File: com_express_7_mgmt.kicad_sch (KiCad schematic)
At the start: 77 parts, among them J12 Plug_Bus_CE7_EPT_401-51501-51, J13 PinHeader_1x3_P2.54mm_Drill1.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, J14 PinHeader_1x3_P2.54mm_Drill1.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, Q11 BSS138-7-F, Q12 BSS138-7-F, SW1 SW_1-1825027-1_THT, U30 74AUP2G132, U31 M24C64-F_DFN8, U32 TPS3840PL30DBVR, U33 74AUP2G132, U34 LTC2950CTS8-1, U36 W25Q32FV_SOIC-8

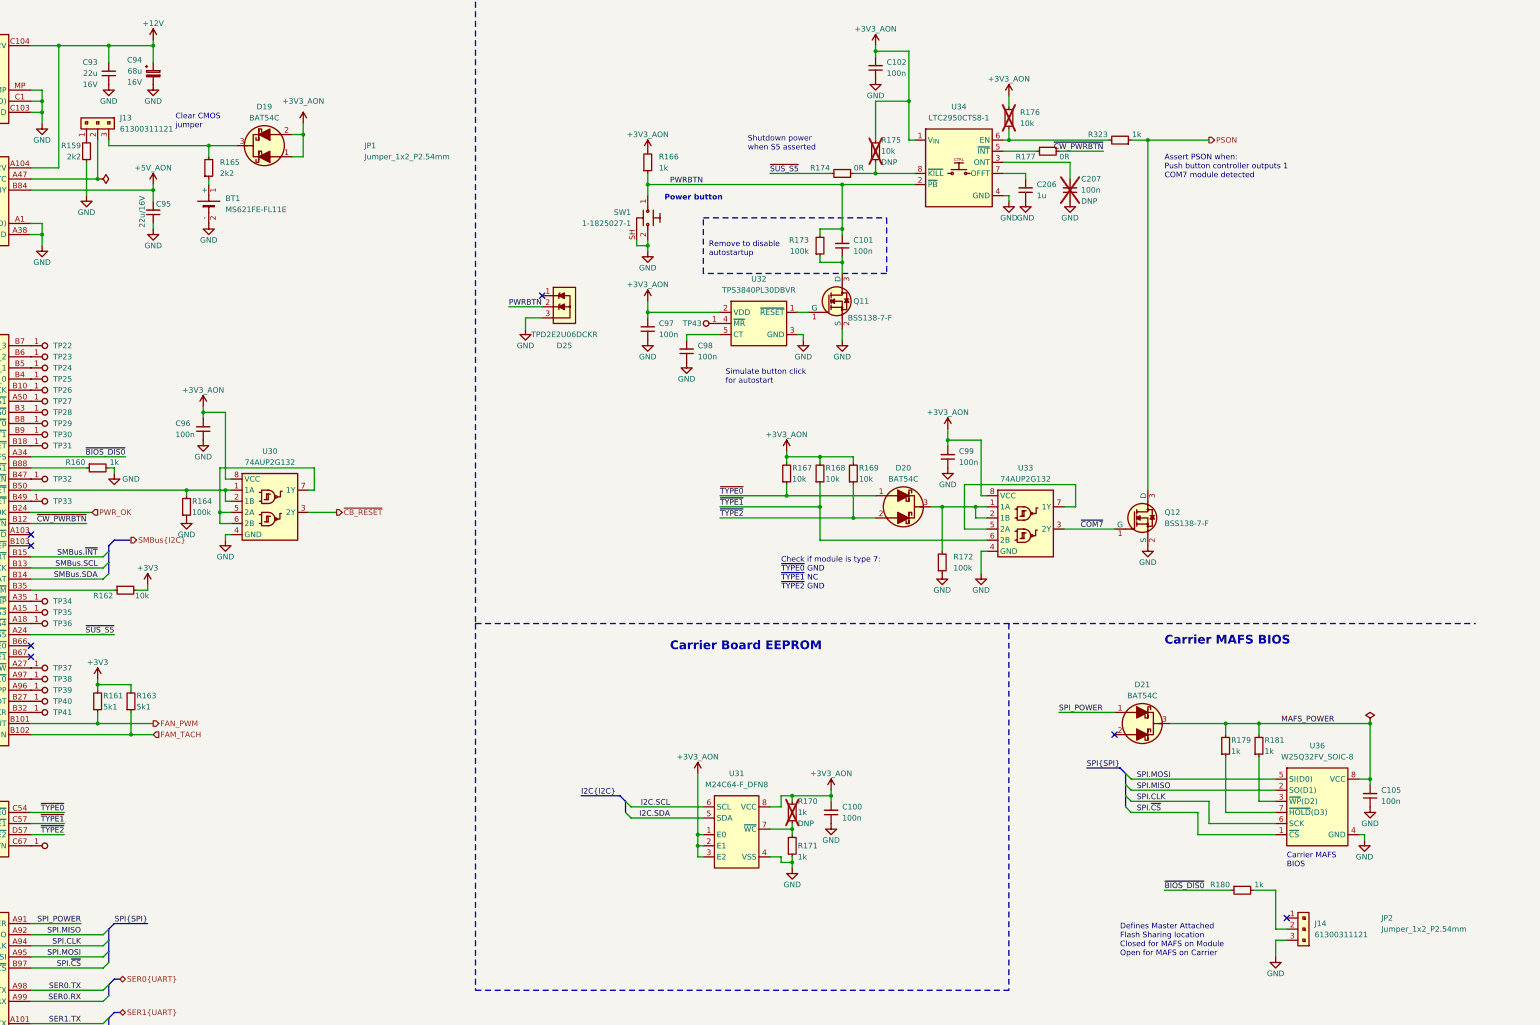
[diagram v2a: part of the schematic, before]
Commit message: Update components from the library
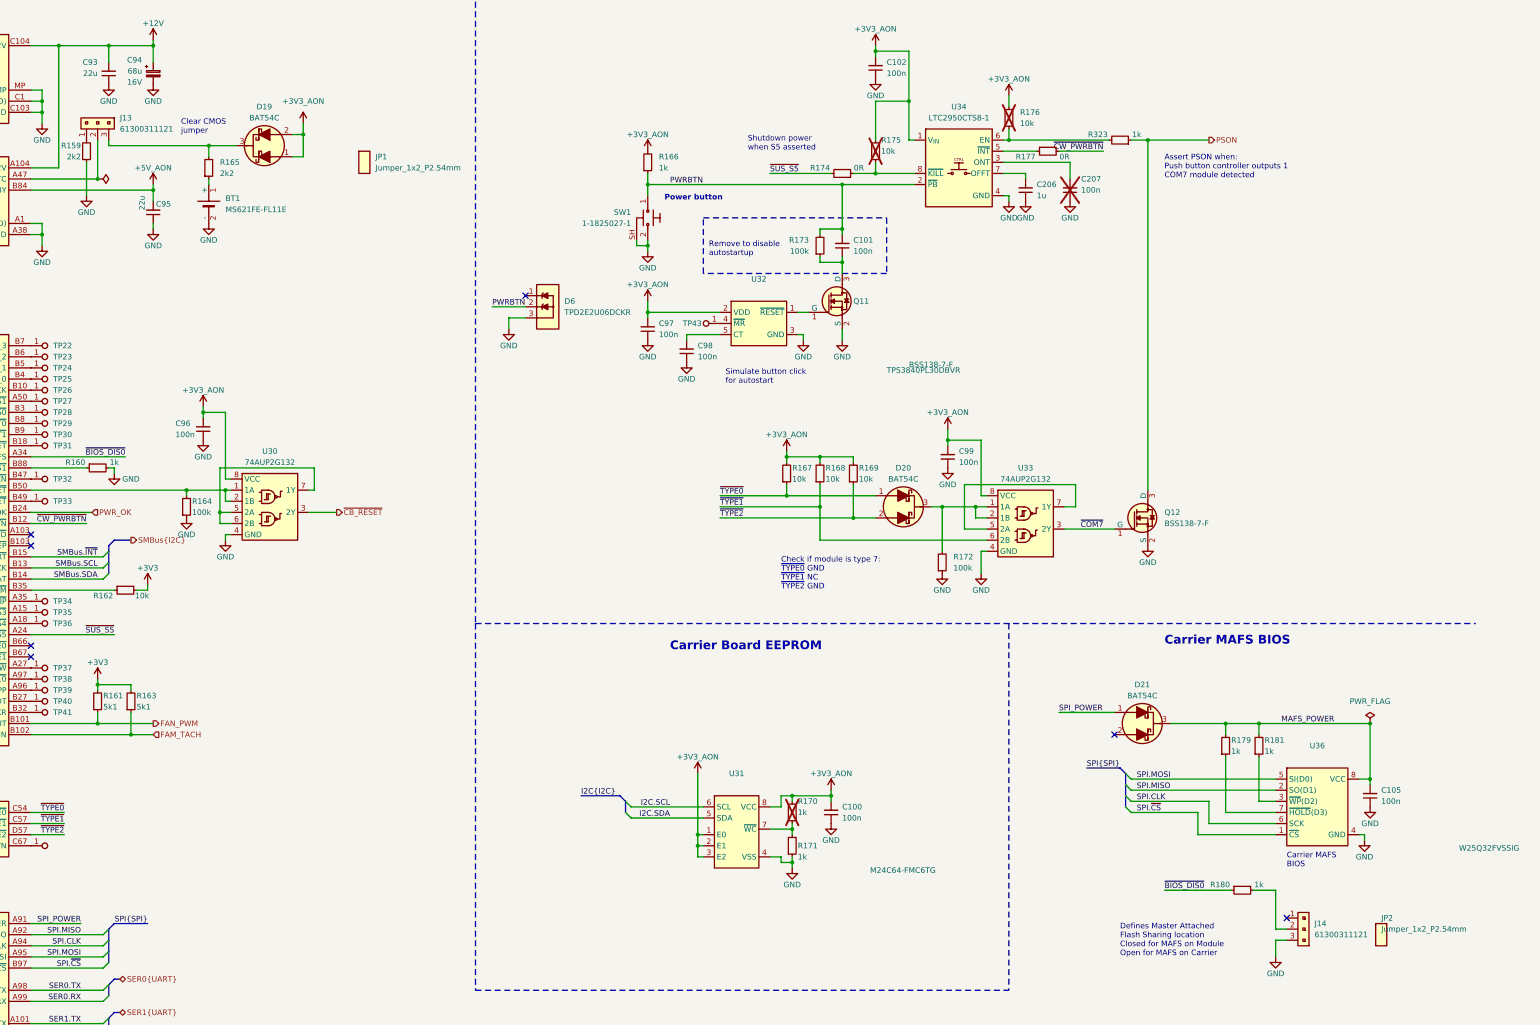
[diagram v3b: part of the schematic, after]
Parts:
- removed D25: TPD2E2U06DCKR, antmicro-footprints:SC70-3, symbol antmicroTVSDiodes:TPD2E2U06DCKR
- added D6: TPD2E2U06_SC70, antmicro-footprints:SC70-3, symbol antmicroTVSDiodes:TPD2E2U06_SC70
- C100, C101, C102, C105, C206, C93, C94, C96, C97, C98, C99, R159, R160, R161, R162, R163, R164, R165, R166, R167, R168, R169, R171, R172, R173, R174, R177, R179, R180, R181, R323, TP22, TP23, TP24, TP25, TP26, TP27, TP28, TP29, TP30, TP31, TP32, TP33, TP34, TP35, TP36, TP37, TP38, TP39, TP40, TP41, TP42, TP43: Public (none) -> False
- C207, R170, R175, R176: DNP DNP -> (none); Public (none) -> False
- C95: Public (none) -> False; Val 22u/16V -> 22u; Voltage (none) -> 16V
- J13, J14: VSD_class IO Header -> (none)
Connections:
- net GND: now also D6.3
- net PWRBTN: now also D6.2

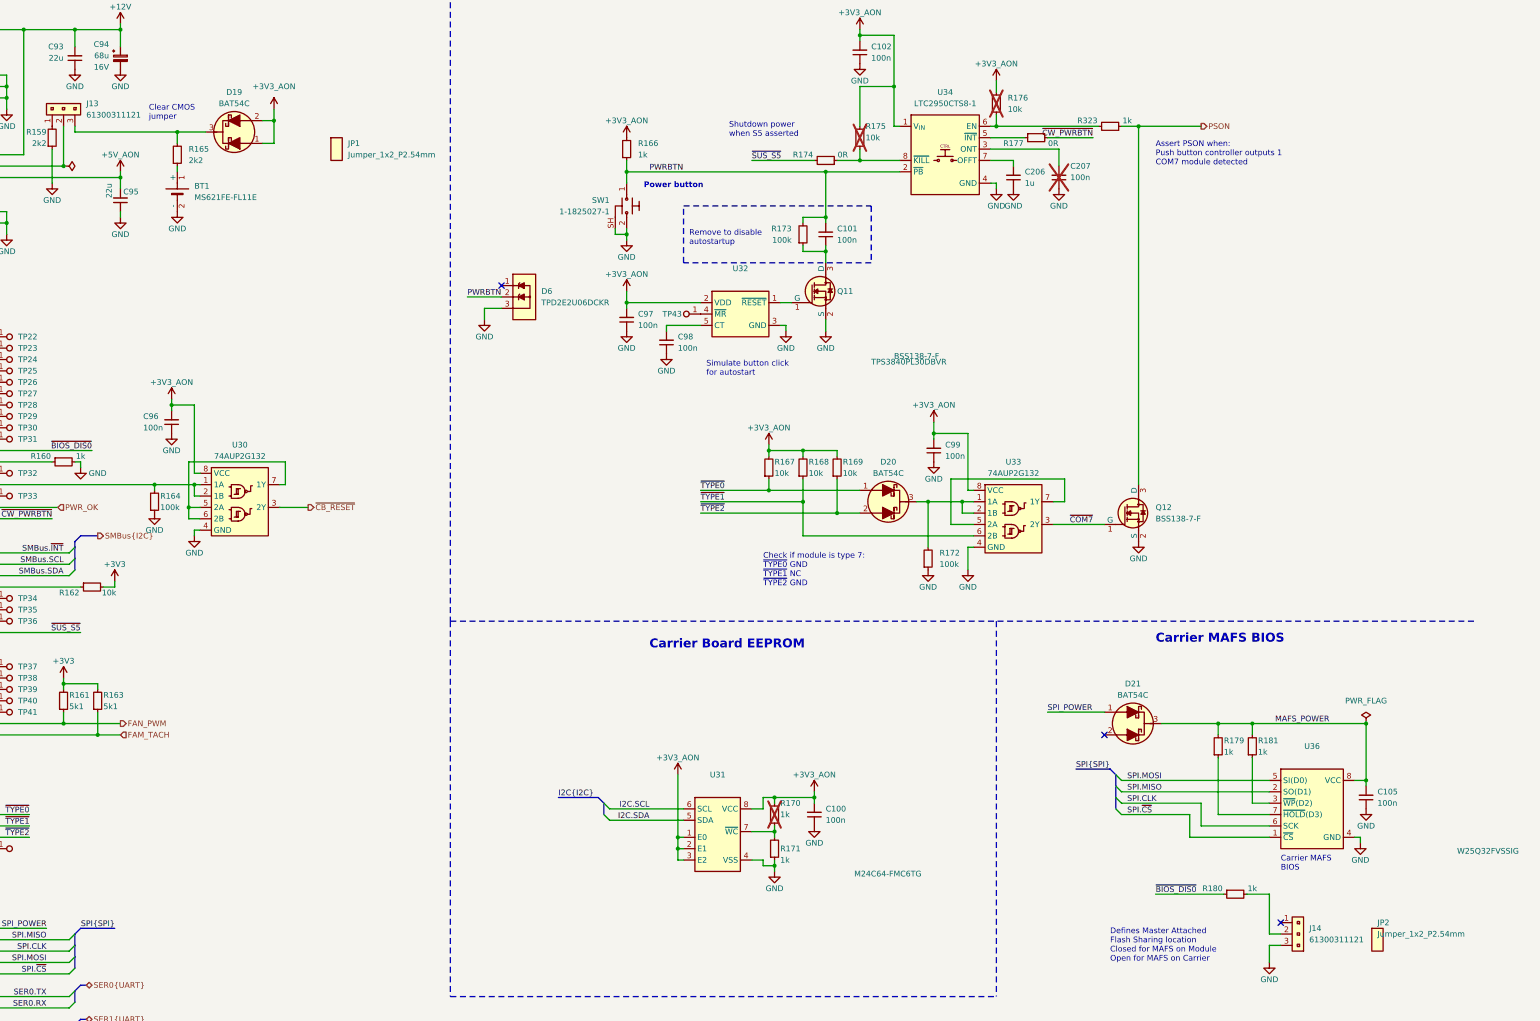
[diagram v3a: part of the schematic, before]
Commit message: [#65447] Fix rotated LEDs, overlapping text and symbols, add rules
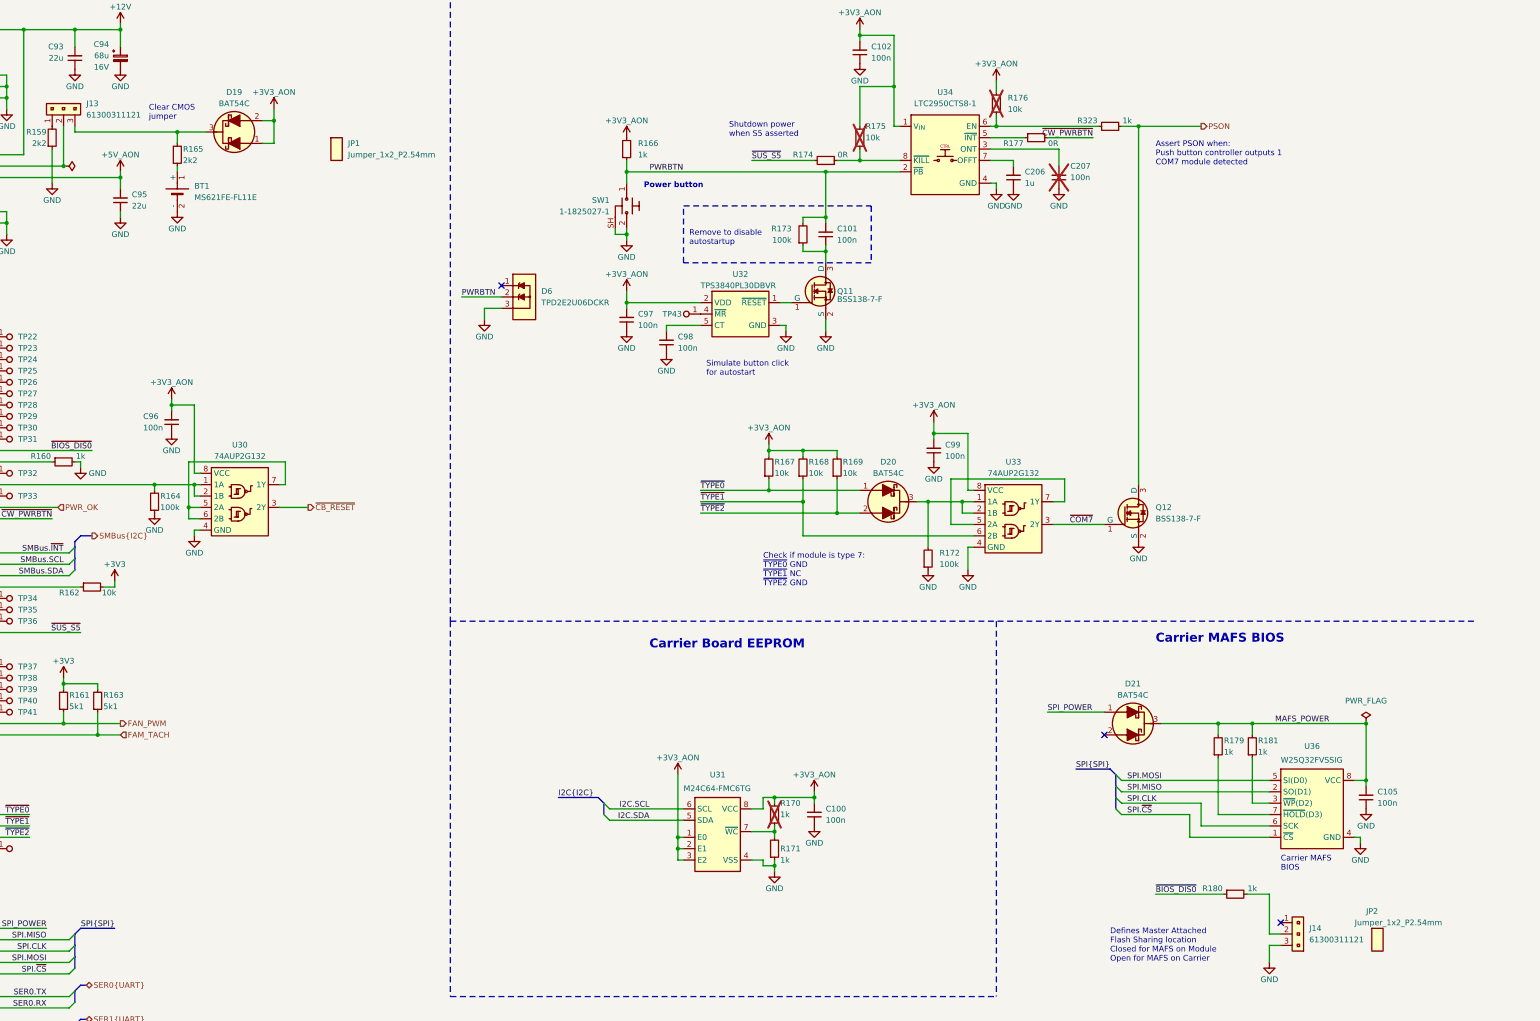
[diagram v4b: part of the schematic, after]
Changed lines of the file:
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@@
     (stroke (width 0) (type default))
   )
-  (bus (pts (xy 99.06 151.13) (xy 95.25 151.13))
+  (bus (pts (xy 97.79 151.13) (xy 95.25 151.13))
     (stroke (width 0) (type default))
   )
@@
     (stroke (width 0) (type default))
   )
-  (wire (pts (xy 181.61 97.79) (xy 189.23 97.79))
+  (wire (pts (xy 180.34 97.79) (xy 189.23 97.79))
     (stroke (width 0) (type default))
   )
@@
     (effects (font (size 1.27 1.27)) (justify right bottom))
   )
-  (label "PWRBTN" (at 181.61 97.79 0) (fields_autoplaced)
+  (label "PWRBTN" (at 180.34 97.79 0) (fields_autoplaced)
     (effects (font (size 1.27 1.27)) (justify left bottom))
   )
@@
     (effects (font (size 1.27 1.27)) (justify left))
   )
-  (hierarchical_label "SMBus{I2C}" (shape output) (at 99.06 151.13 0) (fields_autoplaced)
+  (hierarchical_label "SMBus{I2C}" (shape output) (at 97.79 151.13 0) (fields_autoplaced)
     (effects (font (size 1.27 1.27)) (justify left))
   )
@@
   )
   (symbol (lib_id "antmicroMemory:W25Q32FV_SOIC-8") (at 360.68 205.74 0) (unit 1)
-    (in_bom yes) (on_board yes) (dnp no) (fields_autoplaced)
+    (in_bom yes) (on_board yes) (dnp no)
     (property "Reference" "U36" (at 370.205 198.12 0)
       (effects (font (size 1.27 1.27) (thickness 0.15)))
@@
       (effects (font (size 1.27 1.27) (thickness 0.15)) (justify left bottom) hide)
     )
-    (property "MPN" "W25Q32FVSSIG" (at 402.59 222.25 0)
+    (property "MPN" "W25Q32FVSSIG" (at 363.22 201.93 0)
       (effects (font (size 1.27 1.27) (thickness 0.15)) (justify left bottom))
     )
@@
   )
   (symbol (lib_id "antmicroCapacitors0603:C_22u_16V_0603") (at 104.14 78.74 90) (unit 1)
-    (in_bom yes) (on_board yes) (dnp no)
-    (property "Reference" "C95" (at 104.775 74.295 90)
+    (in_bom yes) (on_board yes) (dnp no) (fields_autoplaced)
+    (property "Reference" "C95" (at 106.68 74.9236 90)
       (effects (font (size 1.27 1.27) (thickness 0.15)) (justify right))
     )
@@
       (effects (font (size 1.27 1.27) (thickness 0.15)) (justify left bottom) hide)
     )
-    (property "Val" "22u" (at 101.6 72.39 0)
+    (property "Val" "22u" (at 106.68 77.4636 90)
       (effects (font (size 1.27 1.27) (thickness 0.15)) (justify right))
     )
@@
   (symbol (lib_id "antmicroBatteryHoldersClipsContacts:Battery_Holder_MS621FE-FL11E") (at 116.84 69.85 0) (unit 1)
     (in_bom yes) (on_board yes) (dnp no) (fields_autoplaced)
-    (property "Reference" "BT1" (at 120.65 73.0249 0)
+    (property "Reference" "BT1" (at 120.65 73.025 0)
       (effects (font (size 1.27 1.27) (thickness 0.15)) (justify left))
     )
@@
       (effects (font (size 1.27 1.27) (thickness 0.15)) (justify left bottom) hide)
     )
-    (property "MPN" "MS621FE-FL11E" (at 120.65 75.5649 0)
+    (property "MPN" "MS621FE-FL11E" (at 120.65 75.565 0)
       (effects (font (size 1.27 1.27) (thickness 0.15)) (justify left))
     )
@@
       (effects (font (size 1.27 1.27) (thickness 0.15)) (justify left bottom) hide)
     )
-    (property "MPN" "BSS138-7-F" (at 276.86 111.76 0)
+    (property "MPN" "BSS138-7-F" (at 264.16 99.06 0)
       (effects (font (size 1.27 1.27) (thickness 0.15)) (justify left bottom))
     )
@@
   )
   (symbol (lib_id "antmicroMemory:M24C64-F_DFN8") (at 229.87 212.09 0) (unit 1)
-    (in_bom yes) (on_board yes) (dnp no) (fields_autoplaced)
+    (in_bom yes) (on_board yes) (dnp no)
     (property "Reference" "U31" (at 237.49 204.47 0)
       (effects (font (size 1.27 1.27) (thickness 0.15)))
@@
       (effects (font (size 1.27 1.27) (thickness 0.15)) (justify left bottom) hide)
     )
-    (property "MPN" "M24C64-FMC6TG" (at 267.97 227.33 0)
+    (property "MPN" "M24C64-FMC6TG" (at 229.87 208.28 0)
       (effects (font (size 1.27 1.27) (thickness 0.15)) (justify left bottom))
     )
@@
   )
   (symbol (lib_id "antmicroResistors0402:R_2k2_0402") (at 116.84 68.58 90) (unit 1)
-    (in_bom yes) (on_board yes) (dnp no) (fields_autoplaced)
-    (property "Reference" "R165" (at 119.38 64.7699 90)
+    (in_bom yes) (on_board yes) (dnp no)
+    (property "Reference" "R165" (at 118.11 64.77 90)
       (effects (font (size 1.27 1.27) (thickness 0.15)) (justify right))
     )
@@
       (effects (font (size 1.27 1.27) (thickness 0.15)) (justify left bottom) hide)
     )
-    (property "Val" "2k2" (at 119.38 67.3099 90)
+    (property "Val" "2k2" (at 118.11 67.31 90)
       (effects (font (size 1.27 1.27) (thickness 0.15)) (justify right))
     )
@@
   )
   (symbol (lib_id "antmicropower:+3V3_AON") (at 138.43 55.88 0) (unit 1)
-    (in_bom yes) (on_board yes) (dnp no) (fields_autoplaced)
+    (in_bom yes) (on_board yes) (dnp no)
     (property "Reference" "#PWR0240" (at 138.43 59.69 0)
       (effects (font (size 1.27 1.27)) hide)
     )
-    (property "Value" "+3V3_AON" (at 138.43 50.8 0)
+    (property "Value" "+3V3_AON" (at 138.43 52.07 0)
       (effects (font (size 1.27 1.27)))
     )
@@
   (symbol (lib_id "antmicroShuntsJumpers:Jumper_1x2_P2.54mm") (at 383.54 238.76 0) (unit 1)
     (in_bom yes) (on_board yes) (dnp no)
-    (property "Reference" "JP2" (at 384.81 237.4899 0)
+    (property "Reference" "JP2" (at 382.27 234.95 0)
       (effects (font (size 1.27 1.27)) (justify left))
     )
-    (property "Value" "Jumper_1x2_P2.54mm" (at 384.81 240.0299 0)
+    (property "Value" "Jumper_1x2_P2.54mm" (at 379.73 237.49 0)
       (effects (font (size 1.27 1.27)) (justify left))
     )
@@
   )
   (symbol (lib_id "antmicroPMICPowerSequencers:TPS3840PL30DBVR") (at 233.68 99.06 0) (unit 1)
-    (in_bom yes) (on_board yes) (dnp no) (fields_autoplaced)
-    (property "Reference" "U32" (at 242.57 91.44 0)
+    (in_bom yes) (on_board yes) (dnp no)
+    (property "Reference" "U32" (at 242.57 92.71 0)
       (effects (font (size 1.27 1.27) (thickness 0.15)))
     )
@@
       (effects (font (size 1.27 1.27) (thickness 0.15)) (justify left bottom) hide)
     )
-    (property "MPN" "TPS3840PL30DBVR" (at 271.78 113.03 0)
-      (effects (font (size 1.27 1.27) (thickness 0.15)) (justify left bottom))
+    (property "MPN" "TPS3840PL30DBVR" (at 233.68 95.25 0)
+      (effects (font (size 1.27 1.27) (thickness 0.15)) (justify left))
     )
     (property "Author" "Antmicro" (at 271.78 115.57 0)
